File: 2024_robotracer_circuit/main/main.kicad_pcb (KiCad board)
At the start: 2 copper layers, 102 parts, among them J1 PH_6p, J10 PH_3p, J11 PH_3p, J12 PH_4p, J14 PH_6p, J2 Conn_02x05_Odd_Even, J3 Conn_02x05_Odd_Even, J4 PA_2p, J5 PA_2p, J6 XT_2p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

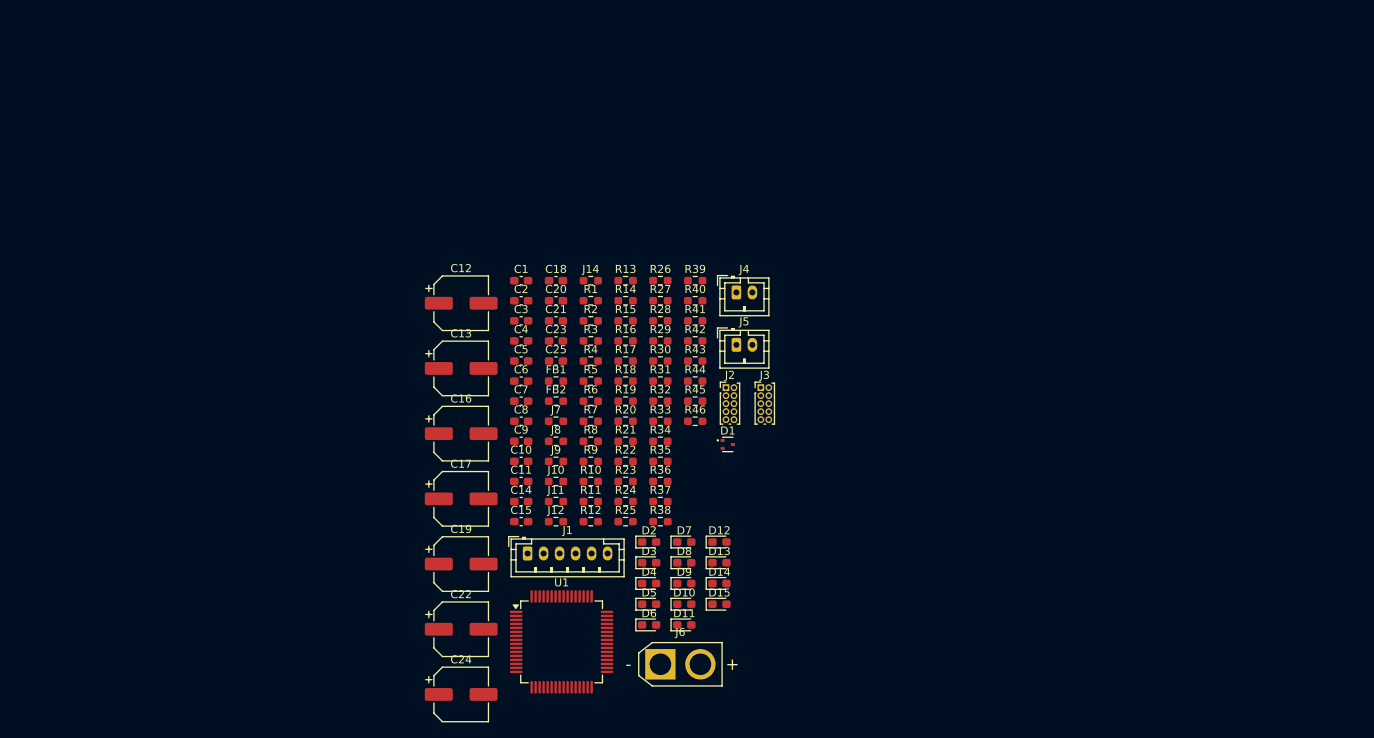
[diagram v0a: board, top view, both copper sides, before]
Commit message: フットプリント割り当ておわり
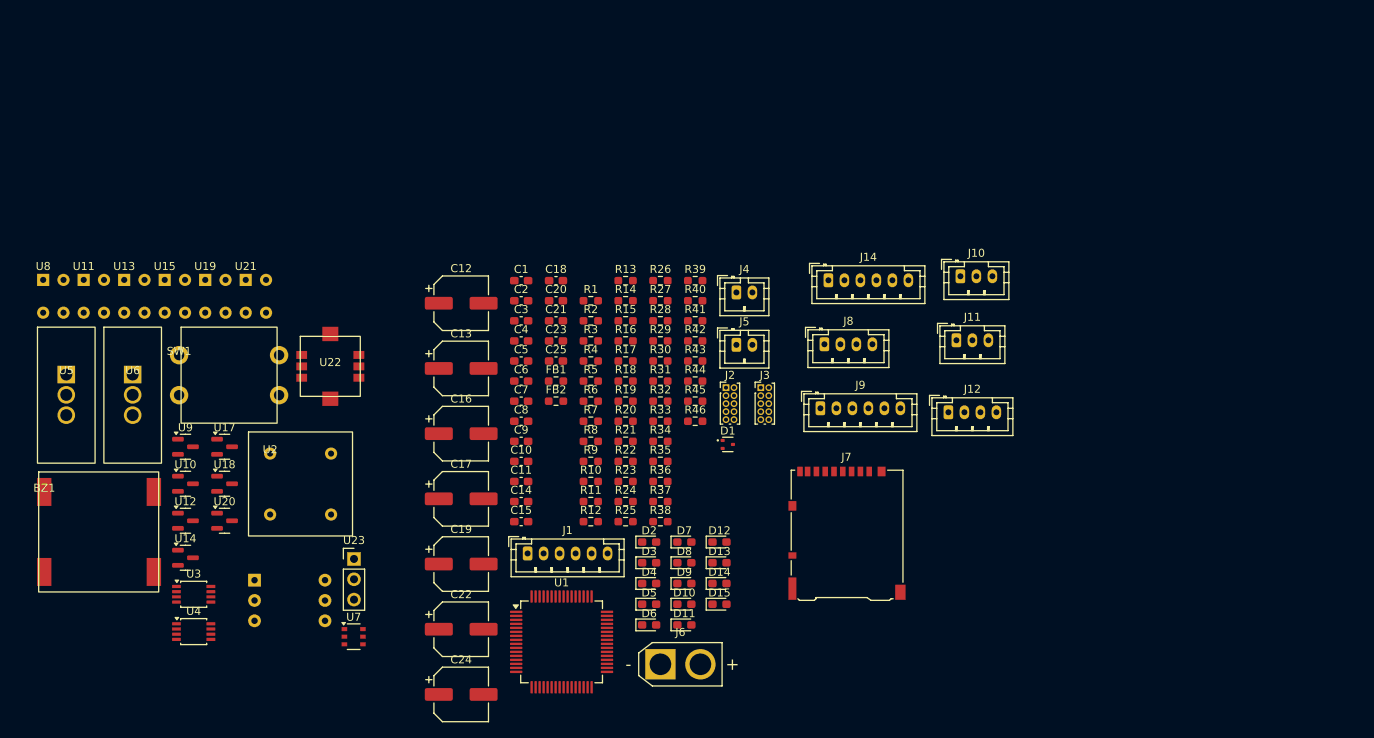
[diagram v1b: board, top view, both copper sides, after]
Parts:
- added BZ1: Buzzer, mylib:UM1515IA085008, F.Cu at (83.0, 95.5)
- added SW1: TVGP01-G73BB, mylib:TVGP01-G73BB, F.Cu at (99.8, 78.4)
- added U10: MTN2306AN3, Package_TO_SOT_SMD:SOT-23, F.Cu at (100.6, 94.4)
- added U11: LBR-127HLD, mylib:LBR-127HLD, F.Cu at (87.9, 69.0)
- added U12: MTN2306AN3, Package_TO_SOT_SMD:SOT-23, F.Cu at (100.6, 99.1)
- added U13: LBR-127HLD, mylib:LBR-127HLD, F.Cu at (93.0, 69.0)
- added U14: MTN2306AN3, Package_TO_SOT_SMD:SOT-23, F.Cu at (100.6, 103.7)
- added U15: LBR-127HLD, mylib:LBR-127HLD, F.Cu at (98.0, 69.0)
- added U16: AE-BMX055, mylib:AE-BMX055, F.Cu at (113.7, 109.3)
- added U17: MTN2306AN3, Package_TO_SOT_SMD:SOT-23, F.Cu at (105.5, 89.8)
- added U18: MTN2306AN3, Package_TO_SOT_SMD:SOT-23, F.Cu at (105.5, 94.4)
- added U19: LBR-127HLD, mylib:LBR-127HLD, F.Cu at (103.1, 69.0)
- added U2: OSC8MI/H, mylib:OSC8MIH, F.Cu at (111.2, 90.7)
- added U20: MTN2306AN3, Package_TO_SOT_SMD:SOT-23, F.Cu at (105.5, 99.1)
- added U21: LBR-127HLD, mylib:LBR-127HLD, F.Cu at (108.2, 69.0)
- added U22: SKRHAAE010, mylib:SKRHAAE010, F.Cu at (118.7, 79.8)
- added U23: SS-22F32G5, Connector_PinHeader_2.54mm:PinHeader_1x03_P2.54mm_Vertical, F.Cu at (121.7, 103.8)
- added U3: AM2837, Package_SO:TSSOP-8_3x3mm_P0.65mm, F.Cu at (101.7, 108.2)
- added U4: AM2837, Package_SO:TSSOP-8_3x3mm_P0.65mm, F.Cu at (101.7, 112.9)
- added U5: BP5293-33, mylib:BP5293-xx, F.Cu at (85.7, 80.8)
- added U6: BP5293-50, mylib:BP5293-xx, F.Cu at (94.0, 80.8)
- added U7: SSM6J808R, Package_SO:TSOP-6_1.65x3.05mm_P0.95mm, F.Cu at (121.7, 113.5)
- added U8: LBR-127HLD, mylib:LBR-127HLD, F.Cu at (82.8, 69.0)
- added U9: MTN2306AN3, Package_TO_SOT_SMD:SOT-23, F.Cu at (100.6, 89.8)
- J10, J11: footprint Resistor_SMD:R_0603_1608Metric_Pad0.98x0.95mm_HandSolder -> Connector_JST:JST_PH_B3B-PH-K_1x03_P2.00mm_Vertical
- J12, J8: footprint Resistor_SMD:R_0603_1608Metric_Pad0.98x0.95mm_HandSolder -> Connector_JST:JST_PH_B4B-PH-K_1x04_P2.00mm_Vertical
- J14, J9: footprint Resistor_SMD:R_0603_1608Metric_Pad0.98x0.95mm_HandSolder -> Connector_JST:JST_PH_B6B-PH-K_1x06_P2.00mm_Vertical
- J7: footprint Resistor_SMD:R_0603_1608Metric_Pad0.98x0.95mm_HandSolder -> Connector_Card:microSD_HC_Hirose_DM3AT-SF-PEJM5
- moved J10 56.7 mm to (197.5, 68.5)
- moved J11 54.0 mm to (197.0, 76.5)
- moved J12 50.9 mm to (196.0, 85.5)
- moved J7 39.0 mm to (183.3, 100.6)
- moved J8 35.7 mm to (180.5, 77.0)
- moved J9 33.7 mm to (180.0, 85.0)
- moved J14 29.7 mm to (181.0, 69.0)

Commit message: 基板わけた
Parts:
- removed D15: LED_Small, LED_SMD:LED_0603_1608Metric_Pad1.05x0.95mm_HandSolder
- removed J11: PH_3p, Connector_JST:JST_PH_B3B-PH-K_1x03_P2.00mm_Vertical
- removed R18, R19, R20, R21, R25, R28: 47k, Resistor_SMD:R_0603_1608Metric_Pad0.98x0.95mm_HandSolder
- removed R26, R29, R9: 4.7, Resistor_SMD:R_0603_1608Metric_Pad0.98x0.95mm_HandSolder
- removed R4: 1k, Resistor_SMD:R_0603_1608Metric_Pad0.98x0.95mm_HandSolder
- removed R46: R_Small, Resistor_SMD:R_0603_1608Metric_Pad0.98x0.95mm_HandSolder
- removed U11, U13, U15, U19, U21: LBR-127HLD, mylib:LBR-127HLD
- removed U12, U14, U18, U20, U9: MTN2306AN3, Package_TO_SOT_SMD:SOT-23
- added J13: PH_8p, Connector_JST:JST_PH_B8B-PH-K_1x08_P2.00mm_Vertical, F.Cu at (158.3, 88.2)
- J10: value PH_3p -> PH_5p; footprint Connector_JST:JST_PH_B3B-PH-K_1x03_P2.00mm_Vertical -> Connector_JST:JST_PH_B5B-PH-K_1x05_P2.00mm_Vertical
- J9: value PH_6p -> PH_5p; footprint Connector_JST:JST_PH_B6B-PH-K_1x06_P2.00mm_Vertical -> Connector_JST:JST_PH_B5B-PH-K_1x05_P2.00mm_Vertical
- R2: value R -> 47k
- R3, R7: value 4.7 -> 47k
- R5: value 4.7 -> 1k
- U10: footprint Package_TO_SOT_SMD:SOT-23 -> Package_TO_SOT_SMD:TSOT-23
- U8: value LBR-127HLD -> MTN2306AN3; footprint mylib:LBR-127HLD -> Package_TO_SOT_SMD:TSOT-23
- moved U8 95.2 mm to (177.1, 55.6)
- moved U3 87.1 mm to (170.9, 55.5)
- moved U4 87.1 mm to (170.9, 60.2)
- moved U10 83.8 mm to (177.1, 60.3)
- moved J14 70.2 mm to (127.6, 114.5)
- moved J6 68.4 mm to (171.1, 49.5)
- moved J10 66.9 mm to (144.2, 108.8)
- moved SW1 57.6 mm to (157.3, 75.1)
- moved D1 53.7 mm to (120.5, 113.8)
- moved U22 52.7 mm to (160.1, 112.5)
- moved J7 51.4 mm to (159.1, 55.3)
- moved C11 48.3 mm to (131.2, 47.2)
- moved C14 48.3 mm to (131.2, 49.7)
- moved C15 48.3 mm to (131.2, 52.2)
- moved U16 48.3 mm to (161.0, 99.8)
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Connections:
- J10 pad 1: +5V -> +3.3V
- J10 pad 2: /SENSOR_L_ADC -> +5V
- J10 pad 3: GND -> /SENSOR_L_ADC
- J9 pad 1: +5V -> +3.3V
- J9 pad 2: /SENSOR0_ADC -> +5V
- J9 pad 3: /SENSOR1_ADC -> /SENSOR_R_ADC
- J9 pad 4: /SENSOR2_ADC -> Net-(J10-Pin_4)
- J9 pad 5: /SENSOR3_ADC -> GND
- R3 pad 1: Net-(U8-cathode) -> /SENSOR_PWM
- R3 pad 2: Net-(U9-D) -> GND
- R36 pad 1: +5V -> +3.3V
- R37 pad 1: +5V -> +3.3V
- R38 pad 1: +5V -> +3.3V
- R39 pad 1: +5V -> +3.3V
- R5 pad 1: Net-(U11-cathode) -> +3.3V
- R5 pad 2: Net-(U10-D) -> /SENSOR_L_ADC
- R6 pad 1: +5V -> +3.3V
- R7 pad 1: Net-(U13-cathode) -> /SENSOR_PWM
- R7 pad 2: Net-(U12-D) -> GND
- U1 pad 2: /LED3 -> /LED2
- U1 pad 28: /LED9 -> /LED8
- U1 pad 3: /LED4 -> /LED3
- U1 pad 33: /LED6 -> /LED5
- U1 pad 4: /LED5 -> /LED4
- U1 pad 40: /LED2 -> /SENSOR_PWM
- U1 pad 45: /LED10 -> /LED9
- U1 pad 56: /LED8 -> /LED7
- U1 pad 57: /LED7 -> /LED6
- U10 pad 1: /SENSOR1_PWM -> /SENSOR_PWM
- U10 pad 2: Net-(U10-D) -> GND
- U10 pad 3: GND -> Net-(J10-Pin_4)
- U17 pad 2: Net-(BZ1--) -> GND
- U17 pad 3: GND -> Net-(BZ1--)
- U8 pad 1: +5V -> /SENSOR_PWM
- U8 pad 2: Net-(U8-cathode) -> GND
- U8 pad 3: GND -> Net-(J13-Pin_7)

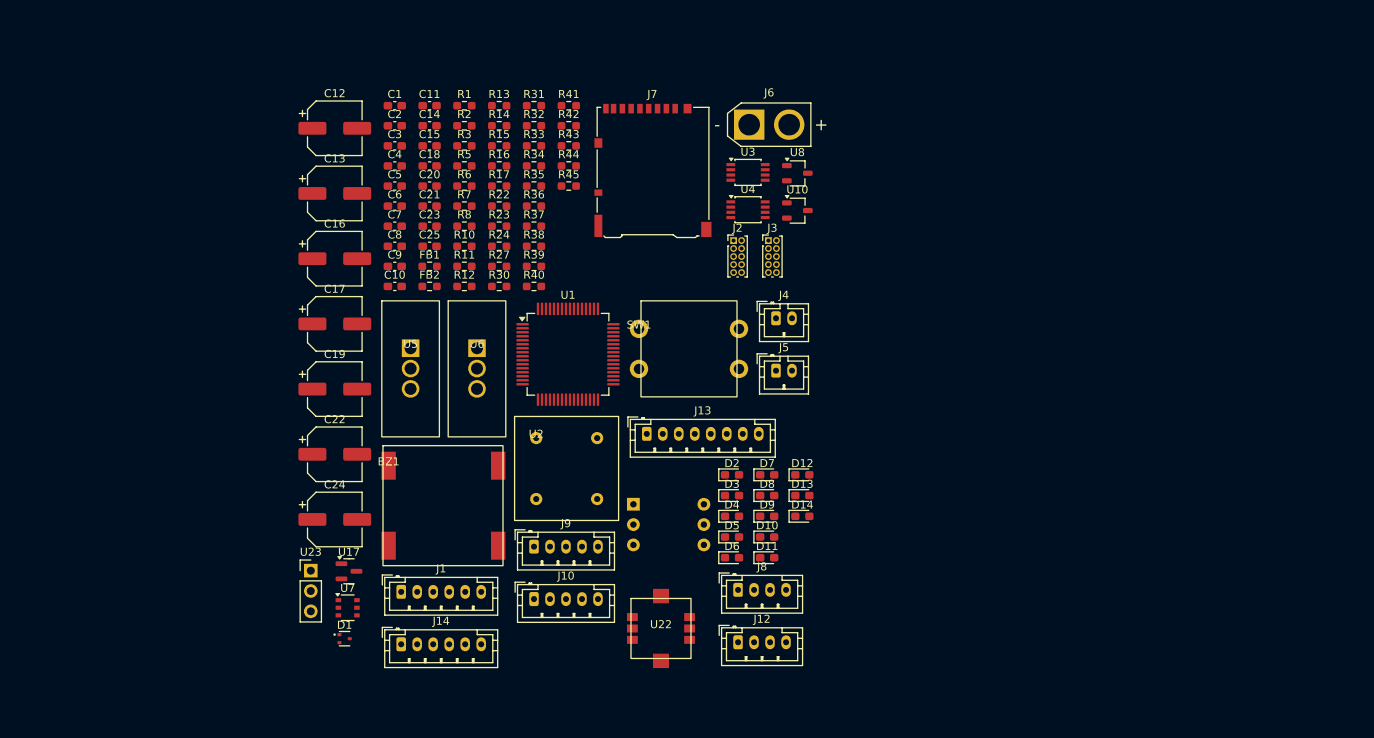
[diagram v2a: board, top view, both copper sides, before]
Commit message: SDカード分けた
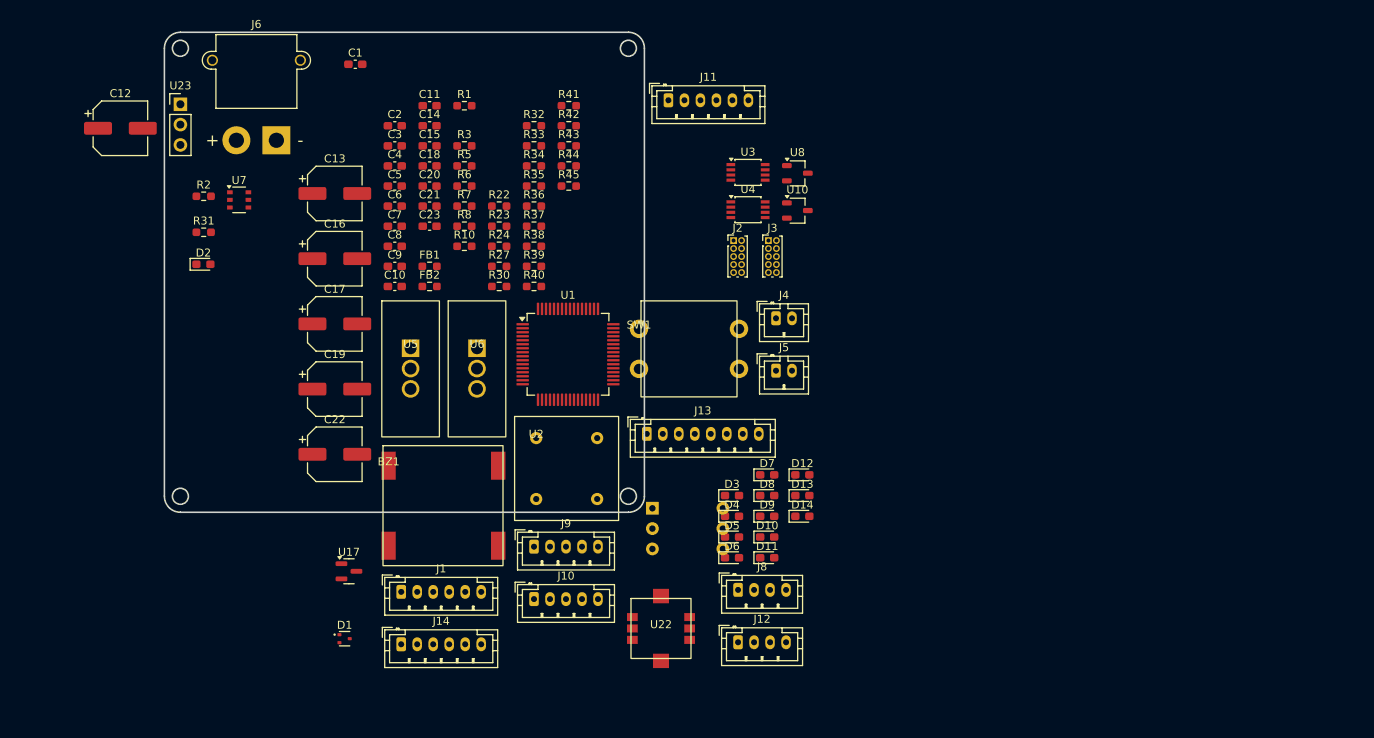
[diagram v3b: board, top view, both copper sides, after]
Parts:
- removed C24: 100u, Capacitor_SMD:CP_Elec_6.3x5.4
- removed C25: 0.1u, Capacitor_SMD:C_0603_1608Metric_Pad1.08x0.95mm_HandSolder
- removed J7: Micro_SD_Card_Det1, Connector_Card:microSD_HC_Hirose_DM3AT-SF-PEJM5
- removed R11, R12, R13, R14, R15, R16, R17: 22k, Resistor_SMD:R_0603_1608Metric_Pad0.98x0.95mm_HandSolder
- added J11: PH_6p, Connector_JST:JST_PH_B6B-PH-K_1x06_P2.00mm_Vertical, F.Cu at (161.0, 46.5)
- J6: footprint Connector_AMASS:AMASS_XT30U-M_1x02_P5.0mm_Vertical -> Connector_AMASS:AMASS_XT30PW-M_1x02_P2.50mm_Horizontal
- moved D2 71.1 mm to (102.9, 67.0)
- moved U23 60.5 mm to (100.0, 47.0)
- moved J6 59.1 mm to (112.0, 51.5)
- moved U7 52.8 mm to (107.3, 59.0)
- moved R31 44.2 mm to (102.9, 63.0)
- moved R2 33.8 mm to (102.9, 58.5)
- moved C12 26.8 mm to (92.5, 50.0)
- moved C1 7.16 mm to (121.9, 42.0)
- moved U16 2.43 mm to (163.4, 100.3)
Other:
- board outline added: 60 x 60 mm

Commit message: パターン引き中
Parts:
- removed C17, C22: 100u, Capacitor_SMD:CP_Elec_6.3x5.4
- U1, U7: moved to B.Cu
- moved U6 34.9 mm to (102.5, 82.4)
- moved C13 34.8 mm to (84.8, 62.5)
- moved U5 29.3 mm to (102.5, 64.5)
- moved C12 23.6 mm to (84.0, 72.0)
- moved C19 22.0 mm to (111.5, 62.0), turned to 180 degrees
- moved D2 21.2 mm to (117.9, 52.0)
- moved R2 20.9 mm to (116.4, 42.5)
- moved R31 20.2 mm to (118.0, 49.5)
- moved C16 14.9 mm to (111.5, 79.0), turned to 180 degrees
- moved C23 14.0 mm to (119.9, 54.0)
- moved U7 9.99 mm to (106.5, 49.0)
- moved U23 9.14 mm to (106.4, 40.5), turned to 90 degrees
- moved U1 5.37 mm to (143.2, 77.2), turned to 180 degrees
- moved J6 3.50 mm to (112.0, 48.0), turned to 90 degrees
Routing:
- net +BATT: track 0.00 -> 69.6 mm, vias 0 -> 7
- net GND: track 0.00 -> 58.4 mm
- net Net-(U7-GATE): track 0.00 -> 8.11 mm
- net Net-(J6-Pin_1): track 0.00 -> 4.36 mm

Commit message: とちゅう
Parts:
- BZ1, C1, C10, C2, C5, C6, C7, C8, C9, R1, SW1, U10, U16, U22, U8: moved to B.Cu
- U7: moved to F.Cu
- moved C12 105.4 mm to (186.7, 95.5)
- moved R41 97.1 mm to (245.5, 52.0)
- moved R42 90.1 mm to (238.6, 52.5)
- moved D10 84.0 mm to (244.5, 56.5)
- moved R43 82.0 mm to (230.6, 52.0)
- moved D11 79.4 mm to (237.6, 57.0)
- moved R44 76.4 mm to (224.9, 52.0)
- moved R8 74.8 mm to (210.1, 56.5)
- moved J12 69.6 mm to (139.5, 51.5), turned to 90 degrees
- moved R45 69.4 mm to (217.9, 56.0)
- moved R10 68.1 mm to (203.1, 56.5)
- moved U16 67.0 mm to (128.0, 43.5), turned to 90 degrees
- moved D3 64.9 mm to (108.4, 72.5)
- moved D5 64.6 mm to (210.4, 51.5)
- moved D12 64.2 mm to (230.4, 56.5)
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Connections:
- U3 pad 5: Net-(J4-Pin_2) -> Net-(J4-Pin_1)
- U3 pad 6: Net-(J4-Pin_2) -> Net-(J4-Pin_1)
- U3 pad 7: Net-(J4-Pin_1) -> Net-(J4-Pin_2)
- U3 pad 8: Net-(J4-Pin_1) -> Net-(J4-Pin_2)
- U4 pad 5: Net-(J5-Pin_2) -> Net-(J5-Pin_1)
- U4 pad 6: Net-(J5-Pin_2) -> Net-(J5-Pin_1)
- U4 pad 7: Net-(J5-Pin_1) -> Net-(J5-Pin_2)
- U4 pad 8: Net-(J5-Pin_1) -> Net-(J5-Pin_2)
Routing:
- net +5V: track 0.00 -> 21.7 mm
- net +BATT: track 69.6 -> 52.4 mm, vias 7 -> 0
- net +3.3V: track 0.00 -> 16.5 mm
- net Net-(U7-GATE): track 8.11 -> 0.00 mm
- net Net-(J5-Pin_1): track 0.00 -> 4.02 mm
- net GND: track 58.4 -> 62.4 mm
- net Net-(J5-Pin_2): track 0.00 -> 3.96 mm
- net Net-(J4-Pin_2): track 0.00 -> 3.86 mm
- net Net-(J4-Pin_1): track 0.00 -> 3.86 mm
- net Net-(J6-Pin_1): track 4.36 -> 3.36 mm
